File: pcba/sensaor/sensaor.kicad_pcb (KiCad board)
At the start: 2 copper layers, 59 x 29.5 mm, 16 parts, among them J1 SAO, J2 WS2812, J3 Conn_01x10_Pin, J4 Conn_01x10_Pin, J5 Conn_01x10_Pin, J6 Programming, J7 Conn_01x10_Pin, J8 Conn_01x10_Pin, J9 Conn_01x10_Pin, U1 CH32V003AxMx

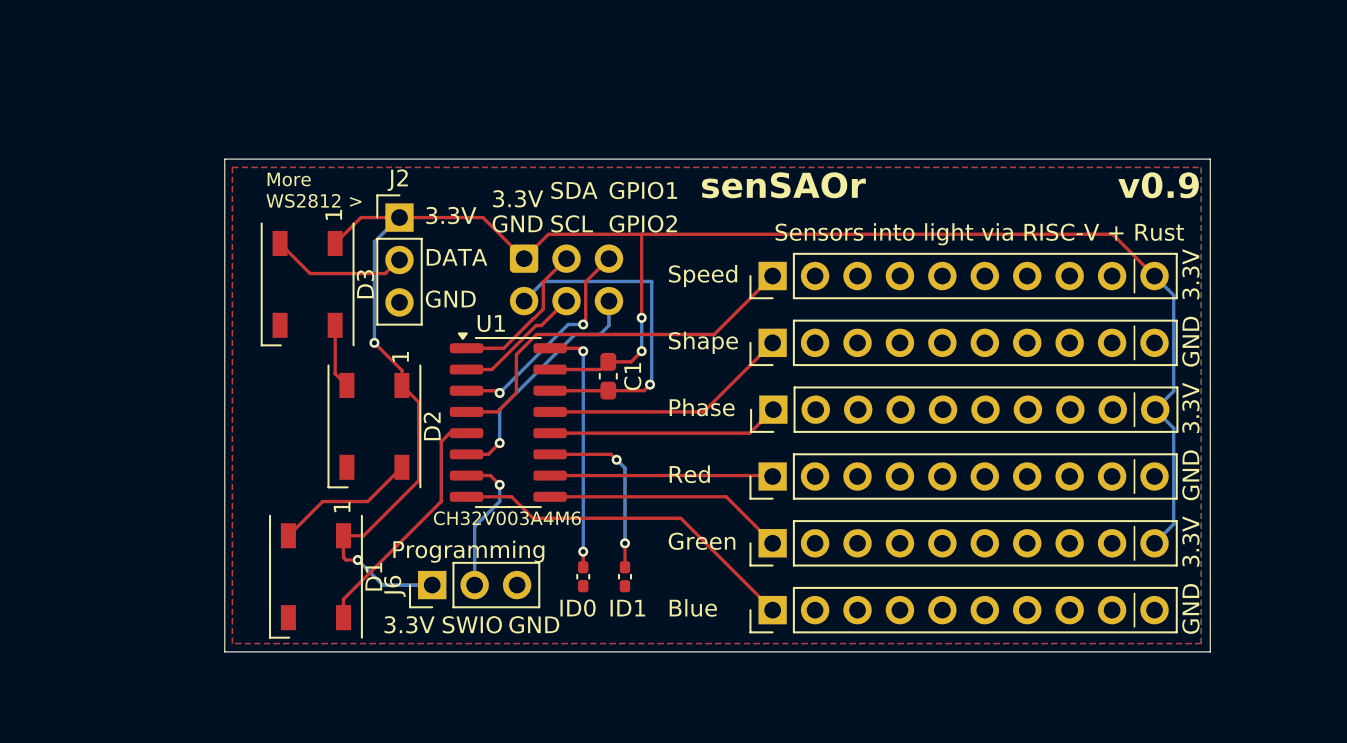
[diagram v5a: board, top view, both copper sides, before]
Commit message: Updates from review feedback, shrunk board more
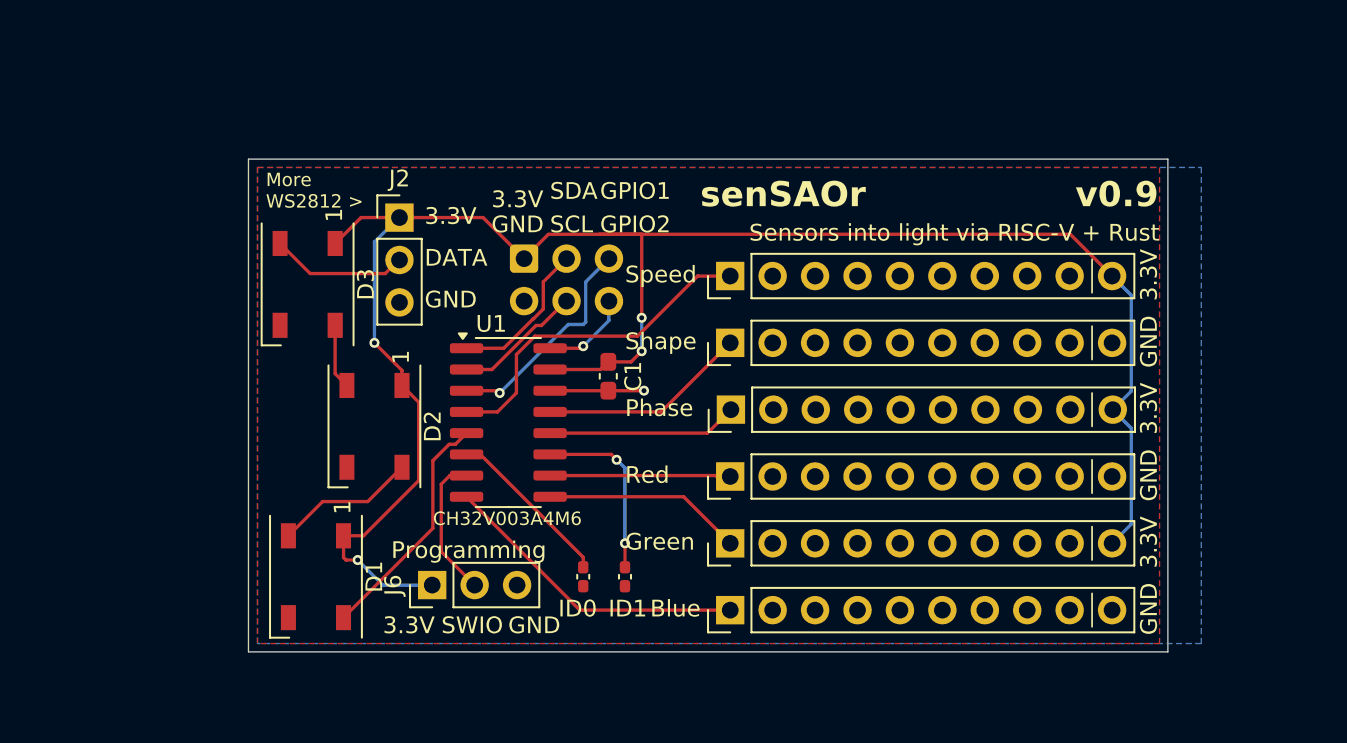
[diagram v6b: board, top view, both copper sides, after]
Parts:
- moved J3 2.54 mm to (104.8, 60.0)
- moved J4 2.54 mm to (104.8, 64.0)
- moved J7 2.54 mm to (104.8, 72.0)
- moved J8 2.54 mm to (104.8, 76.0)
- moved J9 2.54 mm to (104.8, 80.0)
- moved J5 2.54 mm to (104.8, 68.0)
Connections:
- U1 pad 16: /ID0 -> /GPIO2
- U1 pad 6: /GPIO2 -> /ID0
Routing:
- net GND: track 21.5 -> 6.67 mm
- net /GPIO2: track 14.4 -> 5.37 mm
- net /ID0: track 15.1 -> 10.1 mm, vias 2 -> 0
- net /AG: track 14.5 -> 11.9 mm
- net /SPEED: track 23.0 -> 20.5 mm
- net /AB: track 21.1 -> 18.6 mm
- net /SHAPE: track 15.0 -> 12.5 mm
- net /PHASE: track 13.9 -> 11.4 mm
- net /AR: track 13.3 -> 10.9 mm
- net /SWIO: track 8.84 -> 8.60 mm, vias 1 -> 0
- net /GPIO1: vias 2 -> 1
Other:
- board size 59 x 29.5 mm -> 55 x 29.5 mm
